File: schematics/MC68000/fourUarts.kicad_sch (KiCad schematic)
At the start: 36 parts, among them J3 RS232_1, J4 RS232_1, J5 RS232_1, J6 RS232_1, J7 Conn_02x20_Counter_Clockwise, J8 Conn_02x04_Counter_Clockwise, J9 Conn_02x02_Counter_Clockwise, U18_C1 100nf, U18_C2 100nf, U18_C3 100nf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

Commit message: Compilando com linker
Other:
- note added: "U23 e U24 eu tirei, naquele momento eles pareciam estar fazendo algo que dava buss error. eles serão necessários quando for usar as interrupções."
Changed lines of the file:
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@@
     )
+  )
+  (text "U23 e U24 eu tirei, naquele momento eles\npareciam estar fazendo algo que dava buss error.\neles serão necessários quando for usar as \ninterrupções."
+    (at 80.01 191.77 0)
+    (effects (font (size 1.27 1.27)) (justify left bottom))
   )
   (label "RTSA" (at 229.87 62.23 0) (fields_autoplaced)

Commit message: inserido comando vga set_txt_color no 68000
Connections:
- net IRQC: now also U24.2; no longer U24.5
- net IRQD: now also U24.1; no longer U24.4
- net at U24.3: now also U24.1; no longer U24.9
- net at J9.4 (Pin_4): now also U25.2; no longer U25.4
- new net: U24.2, U24.3
- new net: J9.1 (Pin_1), U24.3, U25.1

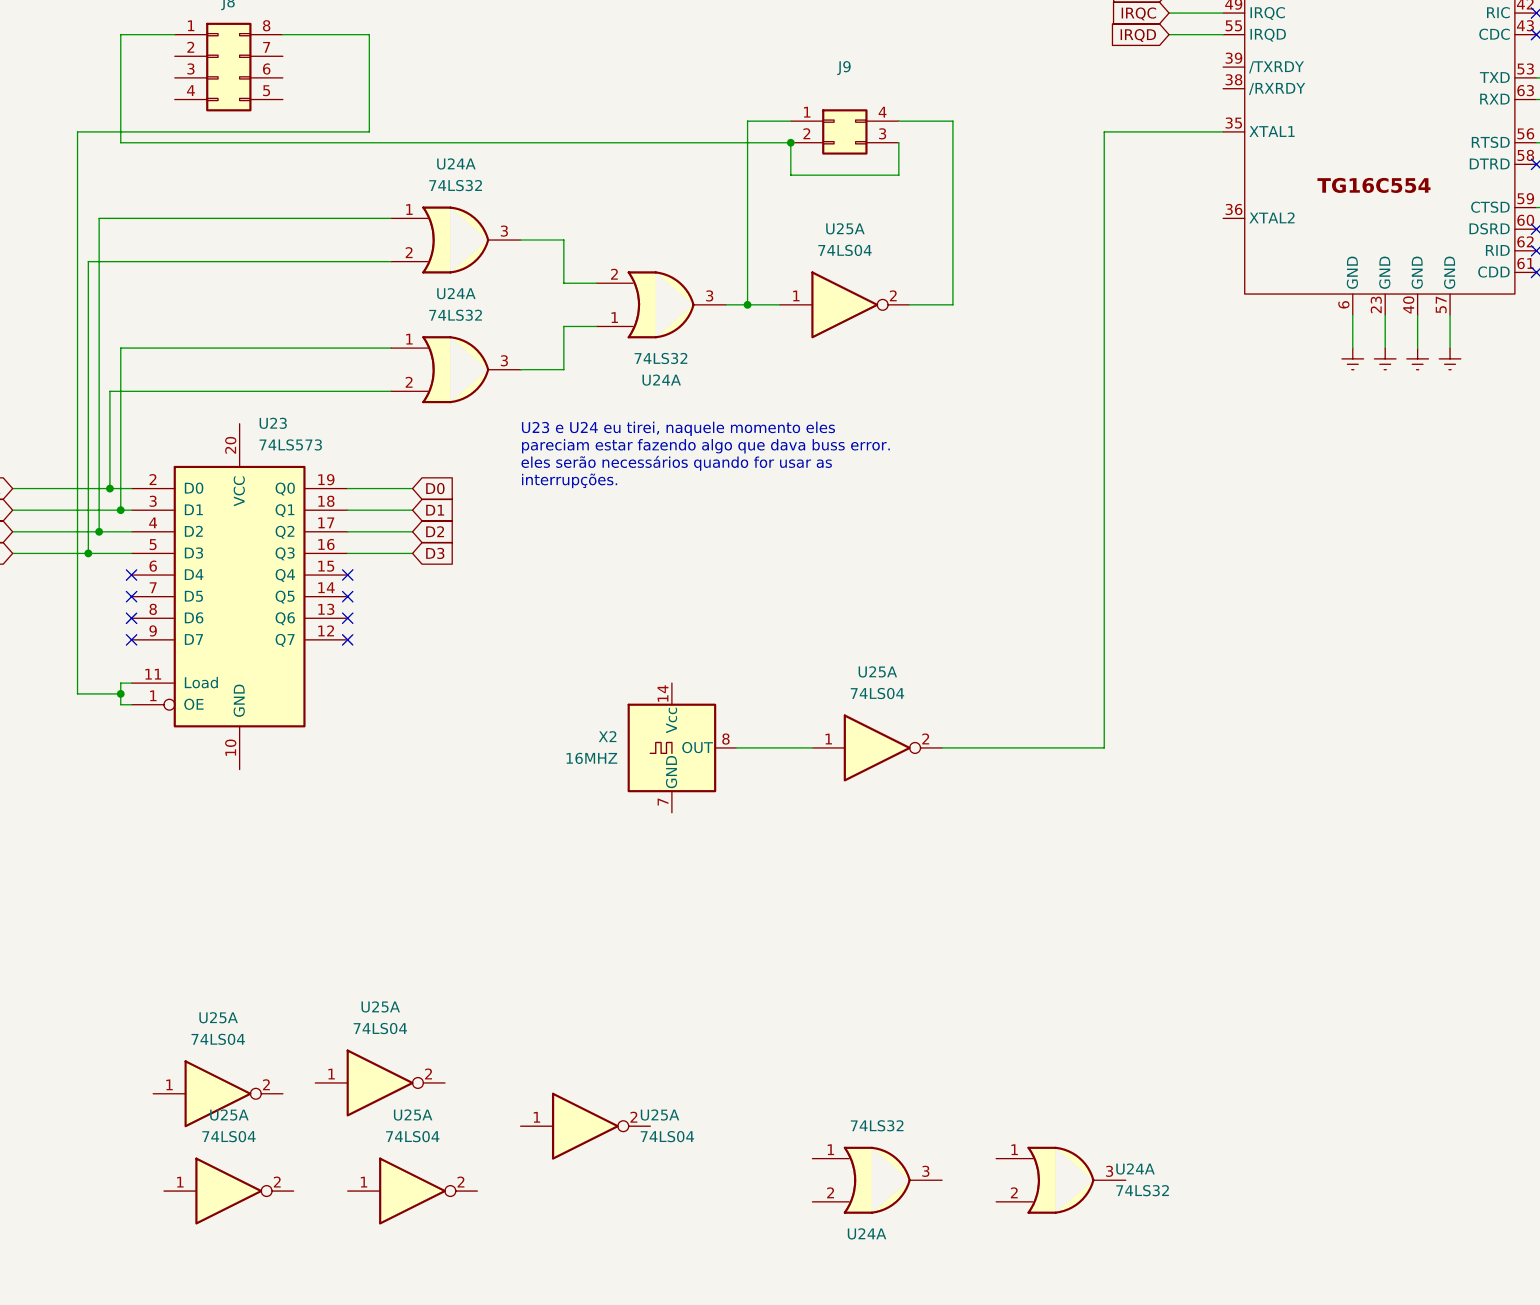
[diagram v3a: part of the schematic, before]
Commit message: fixed uart oscilator in schematic
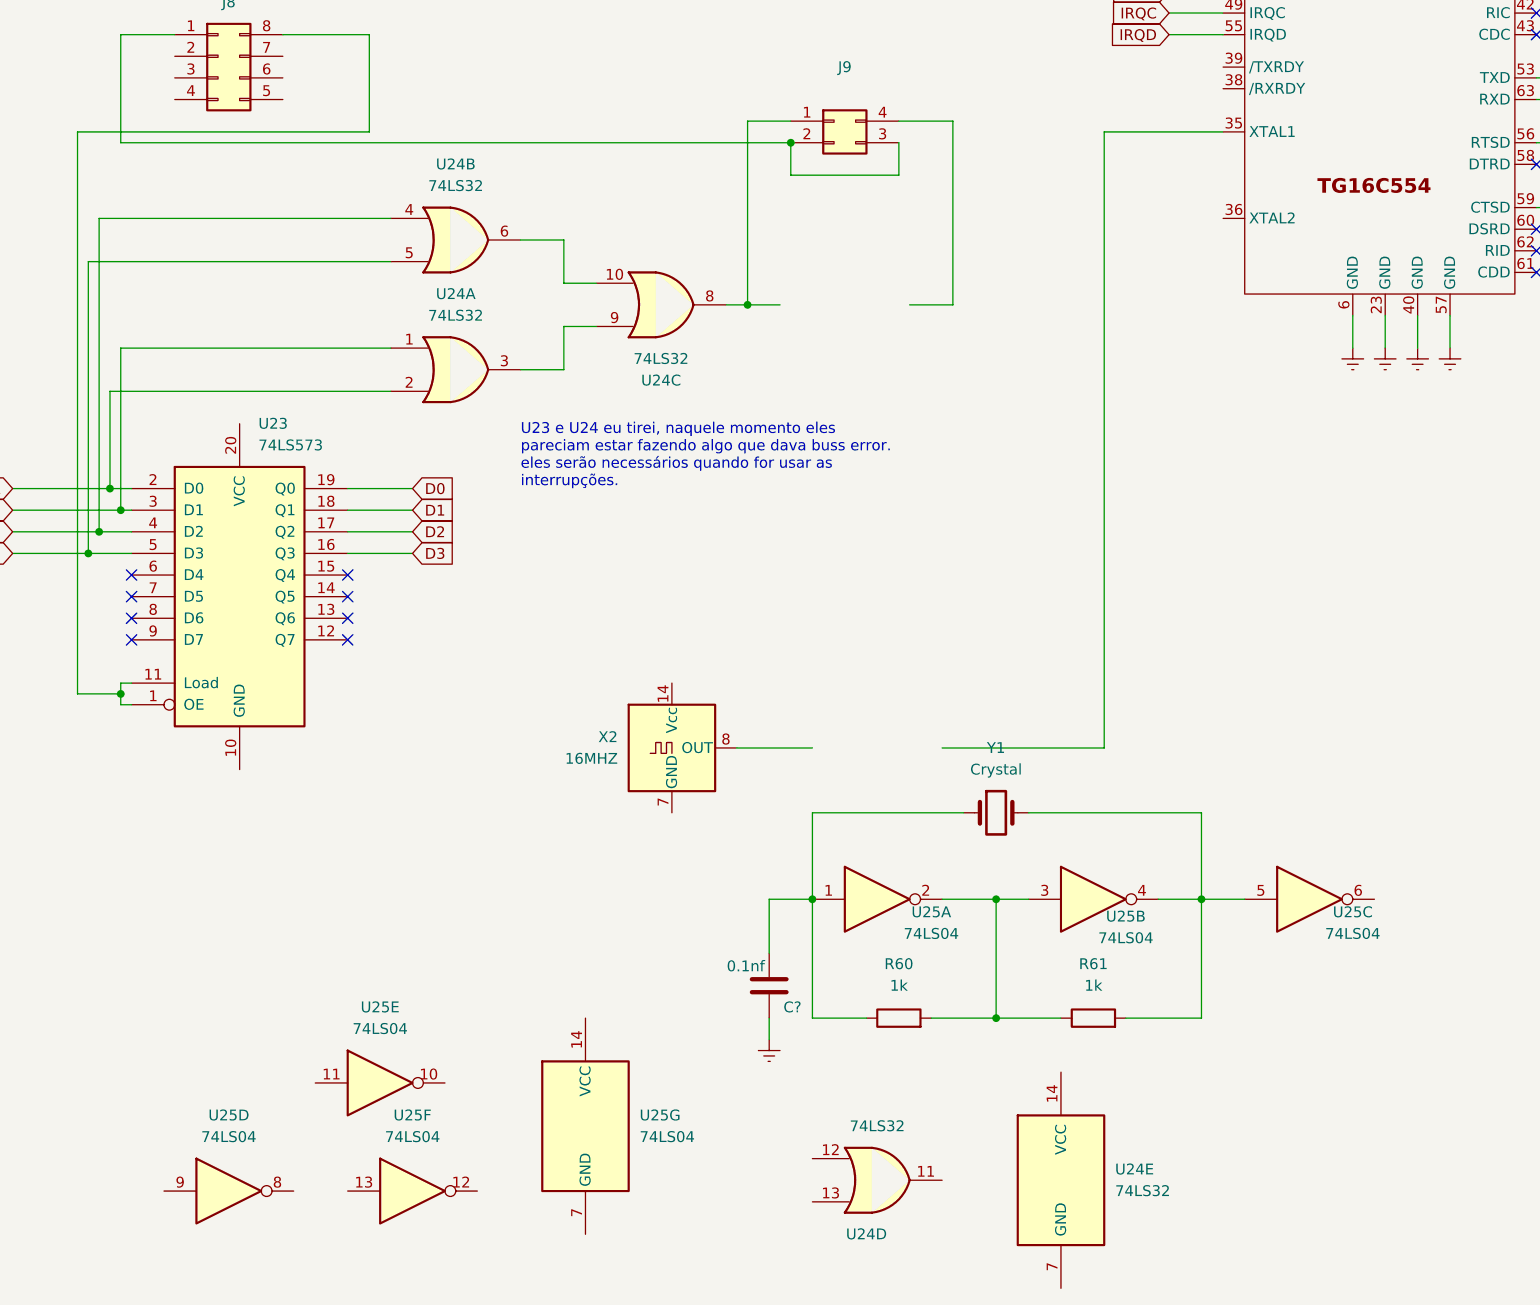
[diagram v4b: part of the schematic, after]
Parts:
- added R60, R61: 1k, symbol Device:R
- added Y1: Crystal, symbol Device:Crystal
- C?: renamed from C8; value 100nf -> 0.1nf
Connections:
- net GNDREF: now also C?.1
- net IRQC: now also U24.5; no longer U24.2
- net IRQD: now also U24.4; no longer U24.1
- net at U24.3: now also U24.9; no longer U24.1
- net at U25.1: now also C?.2, R60.1, Y1.1; no longer X2.8 (OUT)
- net at U25.2: now also U25.3, R60.2, R61.1; no longer U18.35 (XTAL1)
- net at J9.4 (Pin_4): no longer U25.2
- new net: U24.10, U24.6
- new net: J9.1 (Pin_1), U24.8
- new net: R61.2, U25.4, U25.5, Y1.2
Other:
- moved on the sheet: U25A, U25B, U25C

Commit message: updating
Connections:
- net at U25.6: now also U18.35 (XTAL1)
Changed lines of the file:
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@@
+	(wire
+		(pts
+			(xy 185.42 222.25) (xy 185.42 240.03)
+		)
+		(stroke
+			(width 0)
+			(type default)
+		)
+	)
 	(wire
 		(pts
@@
 	(wire
 		(pts
+			(xy 180.34 240.03) (xy 185.42 240.03)
+		)
+		(stroke
+			(width 0)
+			(type default)
+		)
+	)
+	(wire
+		(pts
 			(xy 373.38 95.25) (xy 386.08 95.25)
 		)
@@
 	(wire
 		(pts
-			(xy 129.54 222.25) (xy 148.59 222.25)
-		)
-		(stroke
-			(width 0)
-			(type default)
-		)
-	)
-	(wire
-		(pts
 			(xy 157.48 105.41) (xy 162.56 105.41)
 		)
@@
 		)
 		(stroke
+			(width 0)
+			(type default)
+		)
+	)
+	(wire
+		(pts
+			(xy 148.59 222.25) (xy 185.42 222.25)
+		)
+		(stroke

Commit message: updating
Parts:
- added C?: 0.1nf, symbol Device:C
- C8: renamed from C?; value 0.1nf -> 100nf
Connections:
- net GNDREF: now also C?.1; no longer C8.1
- net at R60.1, U25.1, Y1.1: now also C?.2; no longer C8.2
